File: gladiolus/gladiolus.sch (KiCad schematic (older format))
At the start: 146 parts, among them J1 NEIGHBOR1, J2 NEIGHBOR2, J7 BONUS_ROW, Q1 Q_NPN_BEC, U1 THS4520RGT, U2 AD8330ARQZ, U3 AD9283, U4 AD9704, U5 LMH6643, U6 74LVC1G3157, U7 74LVC1G3157, U8 AT34C02D

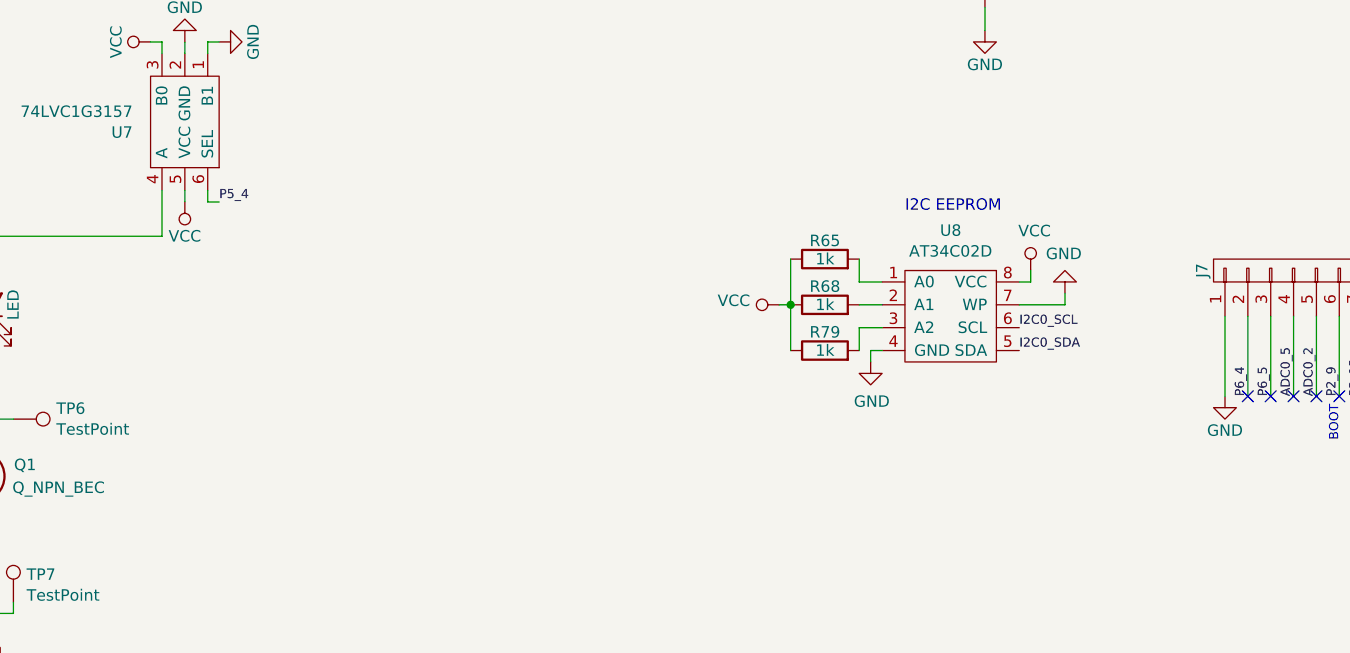
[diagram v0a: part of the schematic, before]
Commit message: Added design notes for test points, EEPROM
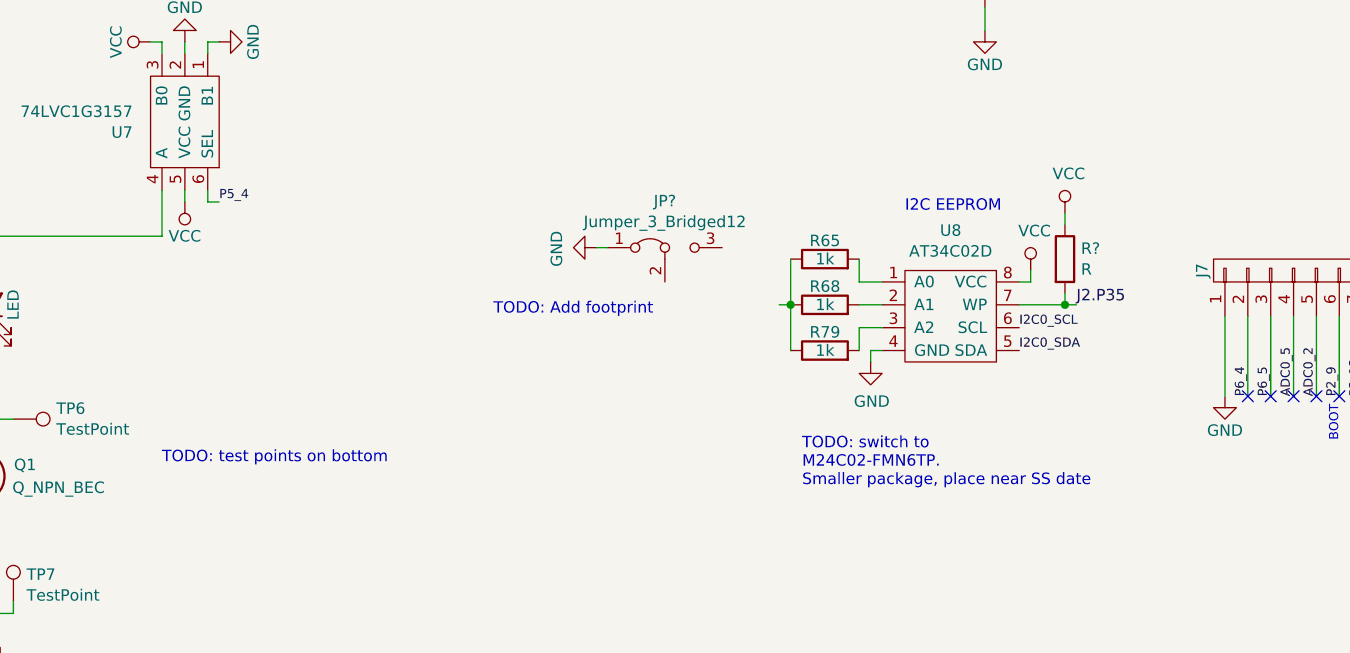
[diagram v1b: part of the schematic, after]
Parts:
- added JP?: Jumper_3_Bridged12, symbol Jumper:Jumper_3_Bridged12
- added R?: R, symbol Device:R
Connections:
- net GND: now also JP?.1 (A); no longer U8.7 (WP)
- net VCC: now also R?.1; no longer R65.1, R68.1, R79.1
- new net: R65.1, R68.1, R79.1
- new net J2.P35: R?.2, U8.7 (WP)
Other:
- note added: "TODO: Add footprint"
- note added: "TODO: switch to \nM24C02-FMN6TP.\nSmaller package, place near SS date"
- note added: "TODO: test points on bottom"
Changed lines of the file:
@@
 Wire Wire Line
 	13400 6550 13400 6500
-$Comp
-L power:GND #PWR088
-U 1 1 5CEA0B08
-P 13550 6600
-F 0 "#PWR088" H 13550 6350 50  0001 C CNN
-F 1 "GND" H 13555 6427 50  0000 C CNN
-F 2 "" H 13550 6600 50  0001 C CNN
-F 3 "" H 13550 6600 50  0001 C CNN
-	1    13550 6600
-	-1   0    0    1
-$EndComp
 Wire Wire Line
 	13550 6650 13550 6600
@@
 Wire Wire Line
 	12650 6650 12750 6650
-$Comp
-L power:VCC #PWR046
-U 1 1 5D1097BE
-P 12300 6650
-F 0 "#PWR046" H 12300 6500 50  0001 C CNN
-F 1 "VCC" V 12318 6777 50  0000 L CNN
-F 2 "" H 12300 6650 50  0001 C CNN
-F 3 "" H 12300 6650 50  0001 C CNN
-	1    12300 6650
-	0    -1   -1   0
-$EndComp
 Wire Wire Line
 	12300 6650 12350 6650
@@
 Wire Wire Line
 	8950 8000 8950 7950
+$Comp
+L power:VCC #PWR?
+U 1 1 5CD84F1F
+P 13550 6250
+F 0 "#PWR?" H 13550 6100 50  0001 C CNN
+F 1 "VCC" H 13567 6423 50  0000 C CNN
+F 2 "" H 13550 6250 50  0001 C CNN
+F 3 "" H 13550 6250 50  0001 C CNN
+	1    13550 6250
+	1    0    0    -1
+$EndComp
+$Comp
+L Device:R R?
+U 1 1 5CD85189
+P 13550 6450
+F 0 "R?" H 13620 6496 50  0000 L CNN
+F 1 "R" H 13620 6405 50  0000 L CNN
+F 2 "" V 13480 6450 50  0001 C CNN
+F 3 "~" H 13550 6450 50  0001 C CNN
+	1    13550 6450
+	1    0    0    -1
+$EndComp
+Wire Wire Line
+	13550 6300 13550 6250
+Wire Wire Line
+	13550 6650 13600 6650
+Connection ~ 13550 6650
+Text Notes 12400 7450 0    50   ~ 0
+TODO: switch to \nM24C02-FMN6TP.\nSmaller package, place near SS date
+Text Label 13600 6650 0    50   ~ 0
+J2.P35
+$Comp
+L power:GND #PWR?
+U 1 1 5CE52474
+P 11500 6400
+F 0 "#PWR?" H 11500 6150 50  0001 C CNN
+F 1 "GND" H 11505 6227 50  0000 C CNN
+F 2 "" H 11500 6400 50  0001 C CNN
+F 3 "" H 11500 6400 50  0001 C CNN
+	1    11500 6400
+	0    1    1    0
+$EndComp
+$Comp
+L Jumper:Jumper_3_Bridged12 JP?
+U 1 1 5CE53BBF
+P 11800 6400
+F 0 "JP?" H 11800 6604 50  0000 C CNN
+F 1 "Jumper_3_Bridged12" H 11800 6513 50  0000 C CNN
+F 2 "" H 11800 6400 50  0001 C CNN
+F 3 "~" H 11800 6400 50  0001 C CNN
+	1    11800 6400
+	1    0    0    -1
+$EndComp
+Wire Wire Line
+	11500 6400 11550 6400
+Text Notes 11050 6700 0    50   ~ 0
+TODO: Add footprint
+Text Notes 9600 7350 0    50   ~ 0
+TODO: test points on bottom
 $EndSCHEMATC

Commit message: Added test points, changed EEPROM package and connections.
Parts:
- removed R65, R68, R79: 1k, gsg-modules:0603, symbol Device:R
- removed R?: R, symbol Device:R
- added JP2, JP3: Jumper_3_Bridged12, Jumper:SolderJumper-3_P1.3mm_Bridged12_RoundedPad1.0x1.5mm_NumberLabels, symbol Jumper:Jumper_3_Bridged12
- added R64: 10k, gsg-modules:0603, symbol Device:R
- added TP10, TP11, TP12, TP13, TP8, TP9: TestPoint, gsg-modules:TESTPOINT-50MIL, symbol Connector:TestPoint
- JP1: renamed from JP?; footprint (none) -> Jumper:SolderJumper-3_P1.3mm_Bridged12_RoundedPad1.0x1.5mm_NumberLabels
- U8: footprint gsg-modules:SOIC8-154 -> Package_SO:TSSOP-8_4.4x3mm_P0.65mm; Description IC EEPROM 2K I2C 1MHZ 8SOIC -> IC EEPROM 2K I2C 400KHZ 8TSSOP; Manufacturer Microchip Technology -> STMicroelectronics; Part Number AT34C02D-SSHM-B -> M24C02-FDW6TP
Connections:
- net J2.P35 is gone; now on net P2_1: U8.7 (WP)
- net GND: now also JP2.1 (A), JP3.1 (A)
- net P2_1: now also R64.2; no longer R77.2
- net P9_5: now also R77.2
- net RXIN: now also TP8.1
- net VCC: now also JP1.3 (B), JP2.3 (B), JP3.3 (B), R64.1
- net at C2.1, L1.2, R6.1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: now also TP10.1
- net at L6.2, U2.12 (OPLO): now also TP13.1
- net at L5.2, U2.13 (OPHI): now also TP12.1
- net at C4.1, L2.2, R11.2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: now also TP11.1
- net at R57.2, U4.24 (FS_ADJ): now also TP9.1
- net at U8.1 (A0): now also JP1.2 (C)
- net at U8.2 (A1): now also JP2.2 (C)
- net at U8.3 (A2): now also JP3.2 (C)
- no-connect marks 60 -> 59
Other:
- note added: "B0: AC coupled\nB1: DC coupled"
- note added: "I2C address selection"
- note removed: "TODO: switch to \nM24C02-FMN6TP.\nSmaller package, place near SS date"
- note removed: "switch for ac/dc coupling\nac coupled on logic low"
- moved on the sheet: JP1, R57

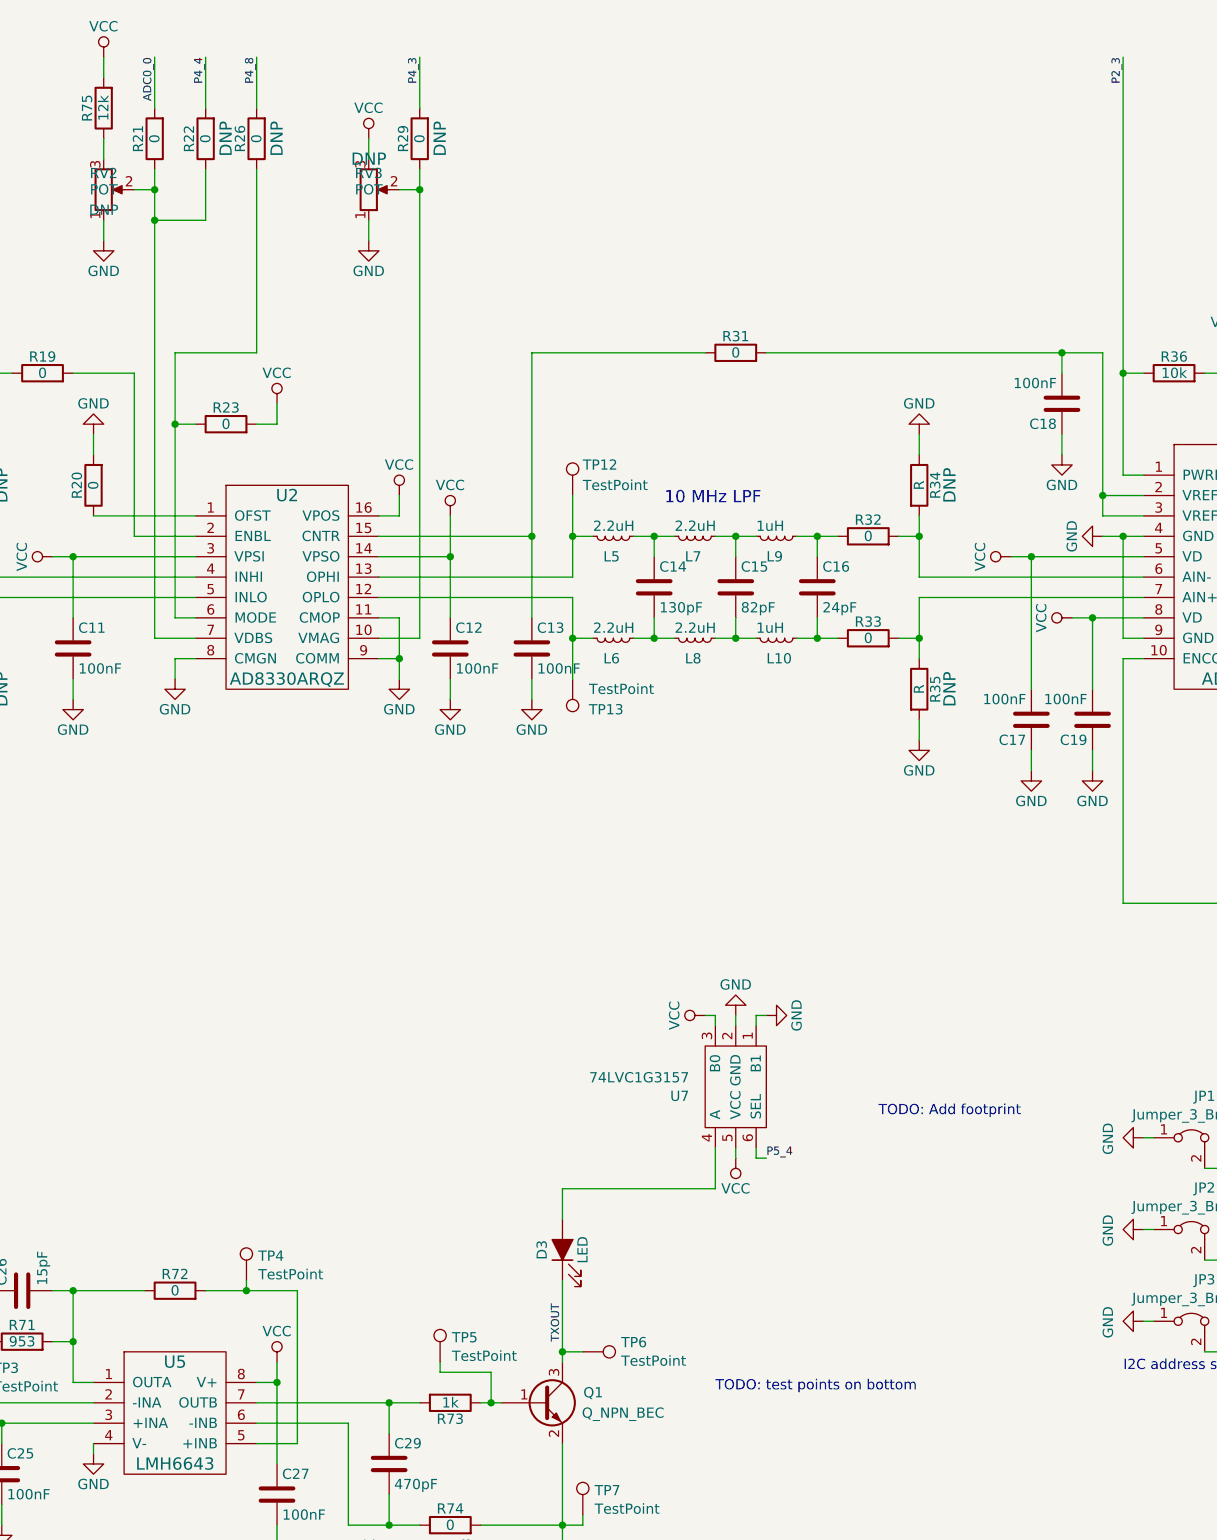
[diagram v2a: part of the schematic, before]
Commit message: Added VDBS voltage range note to schematic
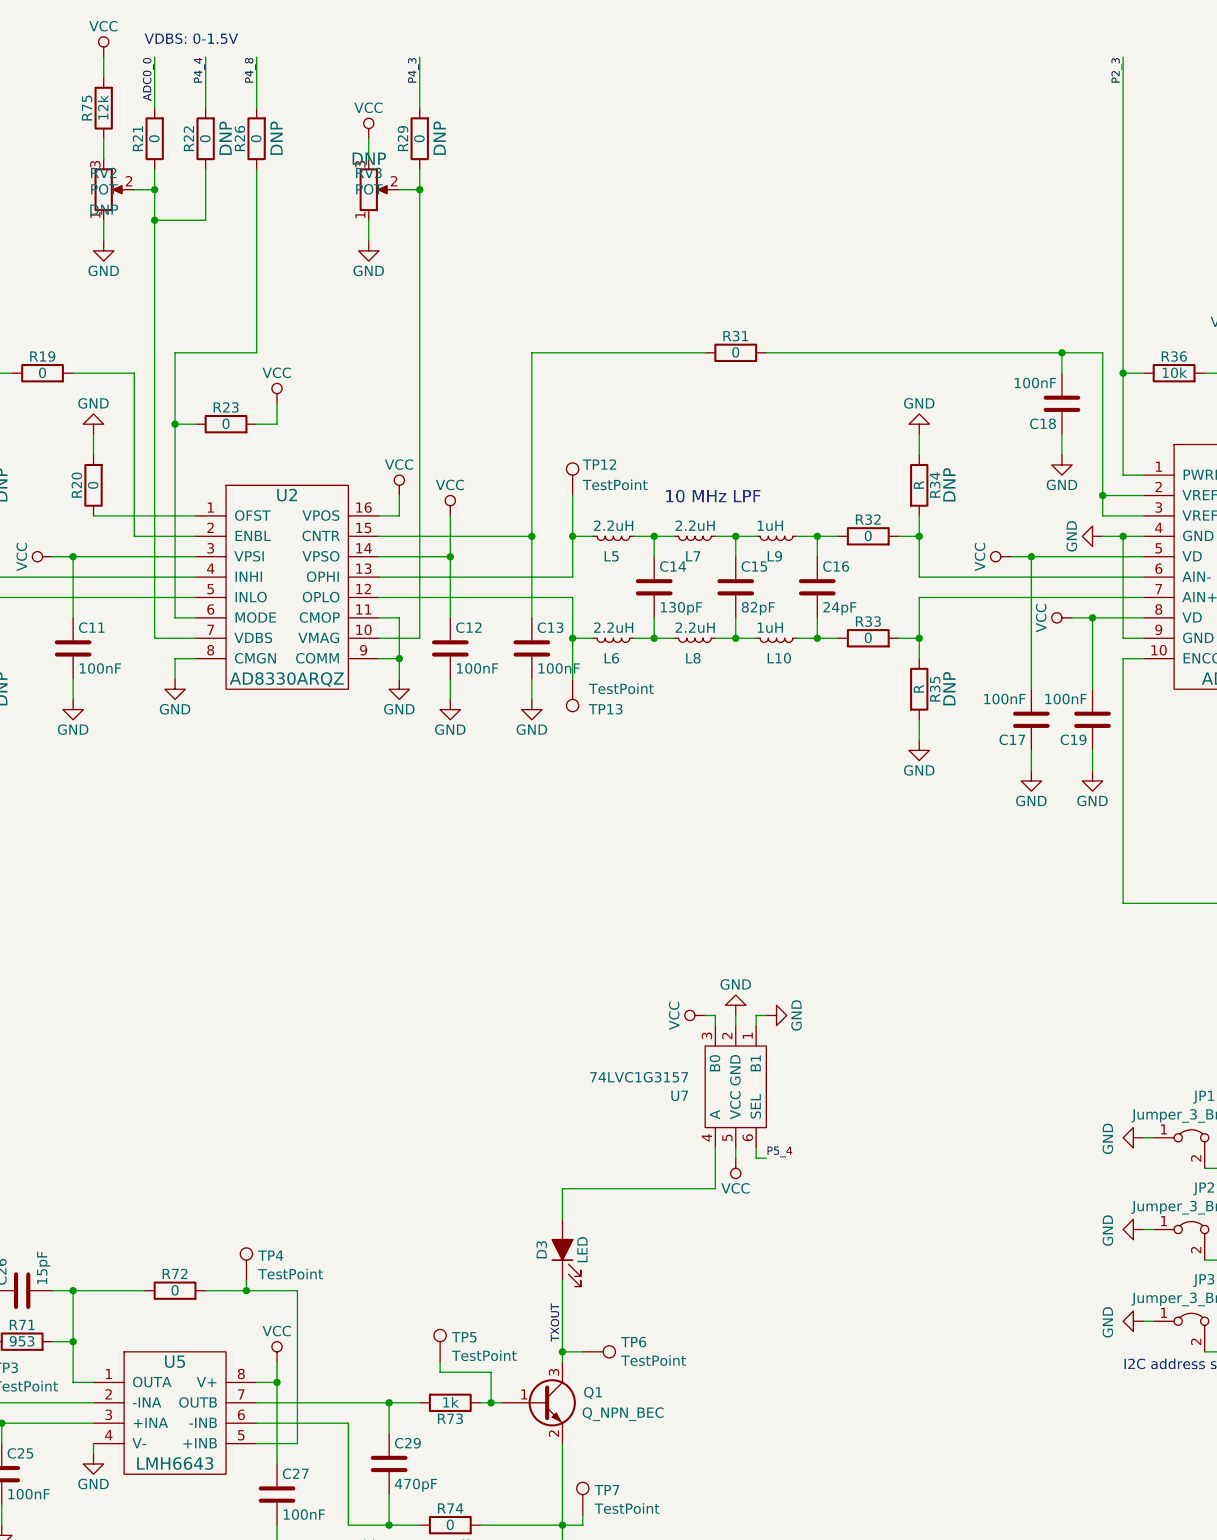
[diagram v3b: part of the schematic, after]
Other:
- note added: "VDBS: 0-1.5V"
- note removed: "TODO: Add footprint"
- note removed: "TODO: test points on bottom"
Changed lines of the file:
@@
 Wire Wire Line
 	11700 6100 11750 6100
-Text Notes 10400 6000 0    50   ~ 0
-TODO: Add footprint
-Text Notes 9600 7350 0    50   ~ 0
-TODO: test points on bottom
 $Comp
 L power:VCC #PWR0112
@@
 Wire Wire Line
 	10600 3450 11700 3450
+Text Notes 6800 750  0    50   ~ 0
+VDBS: 0-1.5V
 $EndSCHEMATC

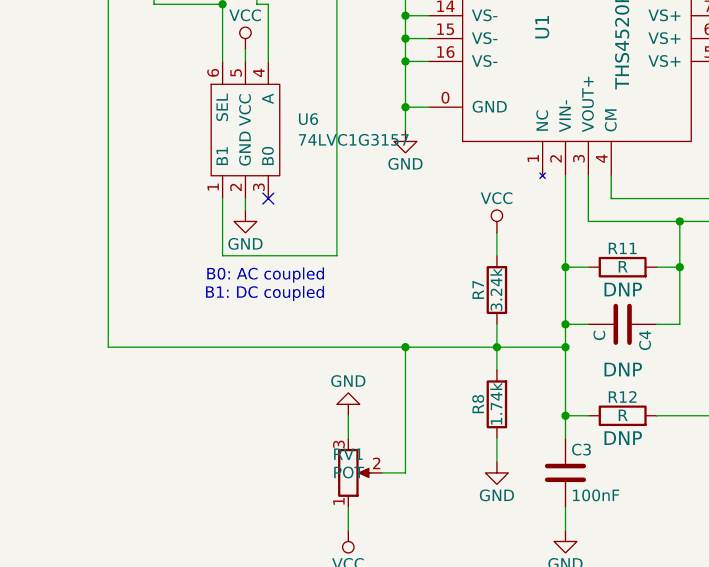
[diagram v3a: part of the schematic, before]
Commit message: Gladiolus: Changed AC/DC coupling note
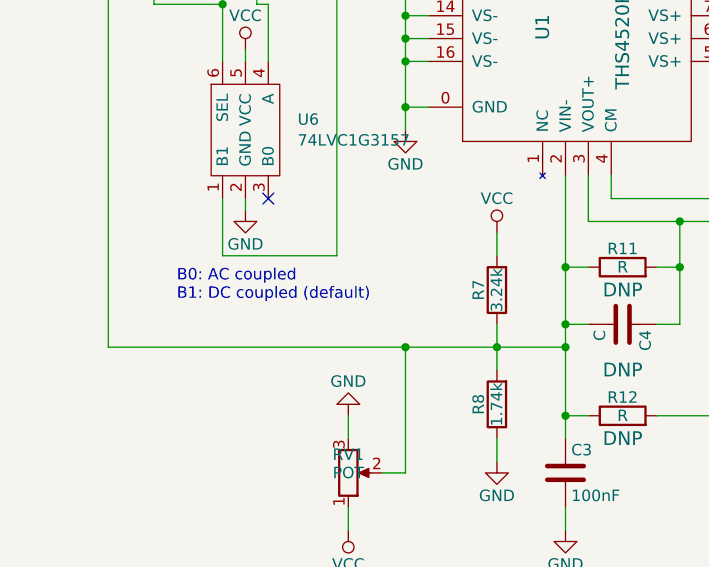
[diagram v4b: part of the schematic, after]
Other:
- note added: "B0: AC coupled\nB1: DC coupled (default)"
- note removed: "B0: AC coupled\nB1: DC coupled"
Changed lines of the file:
@@
 	1650 2650 1650 2700
 Connection ~ 2200 2650
-Text Notes 1850 4600 2    50   ~ 0
-B0: AC coupled\nB1: DC coupled
+Text Notes 1200 4600 0    50   ~ 0
+B0: AC coupled\nB1: DC coupled (default)
 $Comp
 L power:PWR_FLAG #FLG0101
